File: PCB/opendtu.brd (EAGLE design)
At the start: 104.1 x 54 mm, 11 parts, among them M1 DISPLAY-OLED-128X64-I2CNH, M3 NRF24L01-PA-EXT, X1 MCV1,5/2G

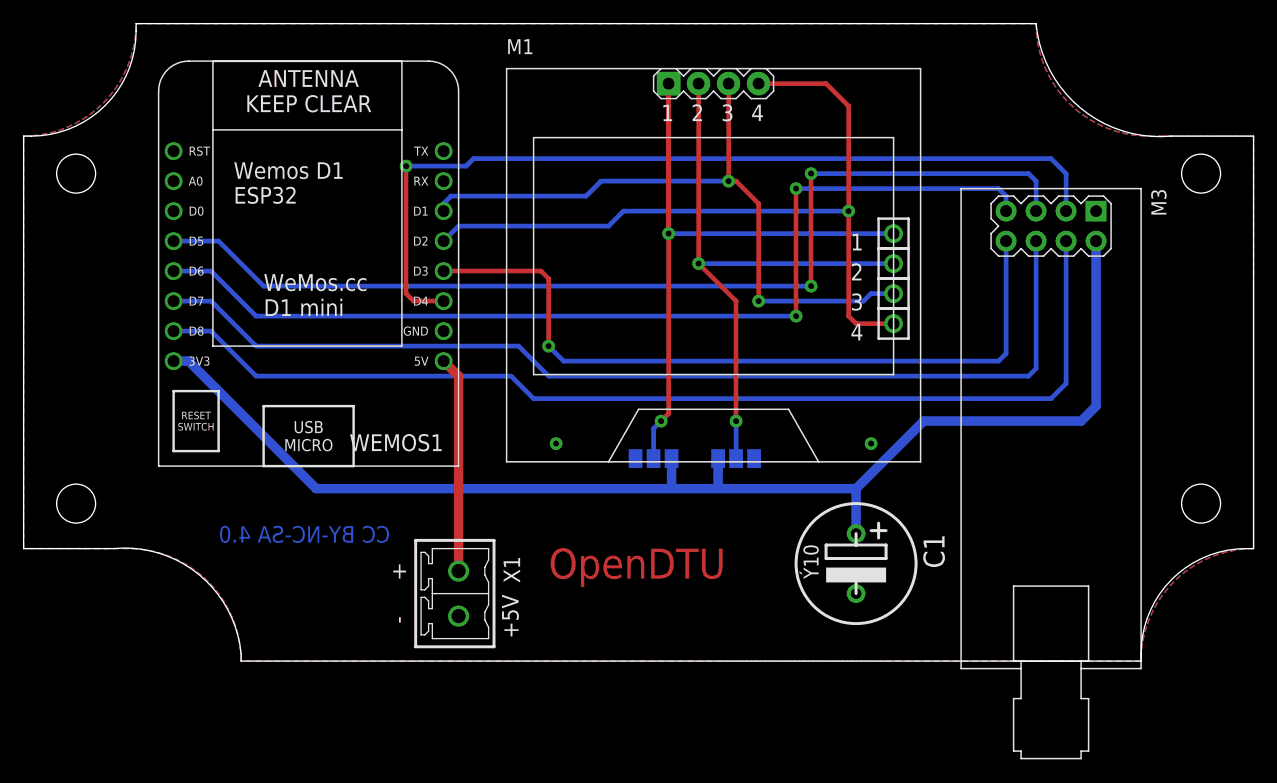
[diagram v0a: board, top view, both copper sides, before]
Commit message: masse
Masse Via hinzugefügt
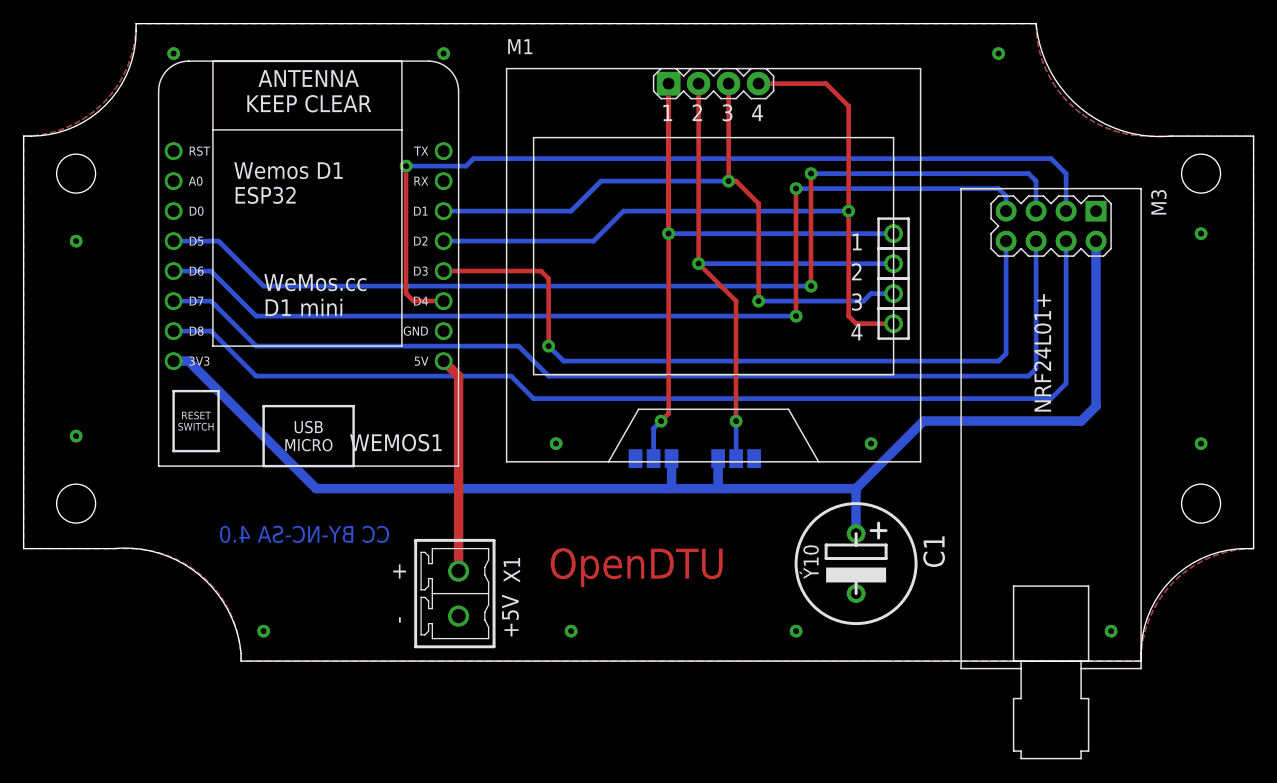
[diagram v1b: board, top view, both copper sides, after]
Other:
- board text added: "NRF24L01+"
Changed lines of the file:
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@@
 <layers>
 <layer number="16" name="Solder" color="1" fill="1" visible="yes" active="yes"/>
-<layer number="1" name="Component" color="4" fill="1" visible="yes" active="yes"/>
+<layer number="1" name="Component" color="4" fill="1" visible="no" active="yes"/>
 <layer number="17" name="Pads" color="2" fill="1" visible="yes" active="yes"/>
 <layer number="18" name="Vias" color="2" fill="1" visible="yes" active="yes"/>
@@
 <text x="59.69" y="46.355" size="1.4" layer="25" ratio="15">3</text>
 <text x="62.23" y="46.355" size="1.4" layer="25" ratio="15">4</text>
+<text x="87.63" y="21.59" size="1.4" layer="25" ratio="15" rot="R90">NRF24L01+</text>
 </plain>
 <attributes>
@@
 <contactref element="M1" pad="4"/>
 <wire x1="71.12" y1="29.21" x2="74.295" y2="29.21" width="0.4" layer="1"/>
-<wire x1="37.465" y1="37.465" x2="50.165" y2="37.465" width="0.4" layer="16"/>
-<wire x1="50.165" y1="37.465" x2="51.435" y2="38.735" width="0.4" layer="16"/>
+<wire x1="48.895" y1="36.195" x2="51.435" y2="38.735" width="0.4" layer="16"/>
 <wire x1="51.435" y1="38.735" x2="70.485" y2="38.735" width="0.4" layer="16"/>
 <via x="70.485" y="38.735" extent="1-16" drill="0.5" diameter="1.1"/>
@@
 <wire x1="70.485" y1="47.625" x2="70.485" y2="38.735" width="0.4" layer="1"/>
 <contactref element="WEMOS1" pad="D2"/>
-<wire x1="36.195" y1="36.195" x2="37.465" y2="37.465" width="0.4" layer="16"/>
+<wire x1="36.195" y1="36.195" x2="48.895" y2="36.195" width="0.4" layer="16"/>
 </signal>
 <signal name="N$2">
 <contactref element="M1" pad="3"/>
 <contactref element="3" pad="1"/>
-<wire x1="36.195" y1="39.37" x2="36.83" y2="40.005" width="0.4" layer="16"/>
-<wire x1="36.83" y1="40.005" x2="48.26" y2="40.005" width="0.4" layer="16"/>
-<wire x1="48.26" y1="40.005" x2="49.53" y2="41.275" width="0.4" layer="16"/>
+<wire x1="36.195" y1="38.735" x2="46.99" y2="38.735" width="0.4" layer="16"/>
+<wire x1="46.99" y1="38.735" x2="49.53" y2="41.275" width="0.4" layer="16"/>
 <wire x1="49.53" y1="41.275" x2="60.325" y2="41.275" width="0.4" layer="16"/>
 <via x="60.325" y="41.275" extent="1-16" drill="0.5" diameter="1.1"/>
@@
 <wire x1="60.96" y1="41.275" x2="60.325" y2="41.275" width="0.4" layer="1"/>
 <contactref element="WEMOS1" pad="D1"/>
-<wire x1="36.195" y1="39.37" x2="36.195" y2="38.735" width="0.4" layer="16"/>
 </signal>
 <signal name="N$3">
@@
 <contactref element="C1" pad="-"/>
 <contactref element="X1" pad="2"/>
-<wire x1="72.39" y1="19.05" x2="91.44" y2="38.735" width="0" layer="19" extent="1-1"/>
-<wire x1="62.484" y1="17.78" x2="72.39" y2="19.05" width="0" layer="19" extent="16-16"/>
-<wire x1="52.451" y1="17.78" x2="62.484" y2="17.78" width="0" layer="19" extent="16-16"/>
-<wire x1="45.72" y1="19.05" x2="52.451" y2="17.78" width="0" layer="19" extent="16-16"/>
-<wire x1="71.12" y1="6.35" x2="72.39" y2="19.05" width="0" layer="19" extent="1-1"/>
-<wire x1="36.195" y1="28.575" x2="45.72" y2="19.05" width="0" layer="19" extent="1-1"/>
-<wire x1="37.465" y1="4.445" x2="45.72" y2="19.05" width="0" layer="19" extent="1-1"/>
+<via x="13.335" y="52.07" extent="1-16" drill="0.5" diameter="1.1"/>
+<via x="83.185" y="52.07" extent="1-16" drill="0.5" diameter="1.1"/>
+<via x="20.955" y="3.175" extent="1-16" drill="0.5" diameter="1.1"/>
+<via x="92.71" y="3.175" extent="1-16" drill="0.5" diameter="1.1"/>
+<via x="5.08" y="19.685" extent="1-16" drill="0.5" diameter="1.1"/>
+<via x="5.08" y="36.195" extent="1-16" drill="0.5" diameter="1.1"/>
+<via x="36.195" y="52.07" extent="1-16" drill="0.5" diameter="1.1"/>
+<via x="100.33" y="36.83" extent="1-16" drill="0.5" diameter="1.1"/>
+<via x="100.33" y="19.05" extent="1-16" drill="0.5" diameter="1.1"/>
+<via x="66.04" y="3.175" extent="1-16" drill="0.5" diameter="1.1"/>
+<via x="46.99" y="3.175" extent="1-16" drill="0.5" diameter="1.1"/>
 </signal>
 </signals>

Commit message: Gerber V1.1
V1.1 vom Gerber
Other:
- board text added: "OpenDTU 3.3.2023 V1.1 Florian Schoop CC BY-NC-SA 4.0"
- board text removed: "OpenDTU 24.2.2023 Florian Schoop CC BY-NC-SA 4.0"
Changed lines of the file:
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@@
 <layers>
 <layer number="16" name="Solder" color="1" fill="1" visible="yes" active="yes"/>
-<layer number="1" name="Component" color="4" fill="1" visible="no" active="yes"/>
+<layer number="1" name="Component" color="4" fill="1" visible="yes" active="yes"/>
 <layer number="17" name="Pads" color="2" fill="1" visible="yes" active="yes"/>
 <layer number="18" name="Vias" color="2" fill="1" visible="yes" active="yes"/>
@@
 J2   2-3  2 +</text>
 <text x="102.87" y="36.195" size="1.4" layer="26" ratio="15" rot="MR270">OpenDTU
-24.2.2023
+3.3.2023 V1.1
 Florian Schoop
 CC BY-NC-SA 4.0</text>
@@
 <text x="62.23" y="46.355" size="1.4" layer="25" ratio="15">4</text>
 <text x="87.63" y="21.59" size="1.4" layer="25" ratio="15" rot="R90">NRF24L01+</text>
+<wire x1="90.17" y1="18.415" x2="90.17" y2="17.145" width="0.4" layer="21"/>
+<wire x1="90.17" y1="17.145" x2="90.17" y2="12.065" width="0.4" layer="21"/>
+<wire x1="90.17" y1="12.065" x2="88.9" y2="12.065" width="0.4" layer="21"/>
+<wire x1="88.9" y1="12.065" x2="88.9" y2="15.875" width="0.4" layer="21"/>
+<wire x1="88.9" y1="15.875" x2="87.63" y2="15.875" width="0.4" layer="21"/>
+<wire x1="87.63" y1="15.875" x2="87.63" y2="12.065" width="0.4" layer="21"/>
+<wire x1="87.63" y1="12.065" x2="86.36" y2="12.065" width="0.4" layer="21"/>
+<wire x1="86.36" y1="12.065" x2="86.36" y2="15.875" width="0.4" layer="21"/>
+<wire x1="86.36" y1="15.875" x2="85.09" y2="15.875" width="0.4" layer="21"/>
+<wire x1="85.09" y1="15.875" x2="85.09" y2="12.065" width="0.4" layer="21"/>
+<wire x1="85.09" y1="12.065" x2="83.82" y2="12.065" width="0.4" layer="21"/>
+<wire x1="83.82" y1="12.065" x2="83.82" y2="15.875" width="0.4" layer="21"/>
+<wire x1="83.82" y1="15.875" x2="82.55" y2="15.875" width="0.4" layer="21"/>
+<wire x1="82.55" y1="15.875" x2="82.55" y2="12.065" width="0.4" layer="21"/>
+<wire x1="82.55" y1="12.065" x2="80.01" y2="12.065" width="0.4" layer="21"/>
+<wire x1="83.82" y1="17.145" x2="90.17" y2="17.145" width="0.4" layer="21"/>
+<wire x1="80.01" y1="17.78" x2="95.25" y2="17.78" width="0.1" layer="21"/>
+<wire x1="80.01" y1="11.43" x2="95.25" y2="11.43" width="0.1" layer="21"/>
 </plain>
 <attributes>
@@
 <via x="66.04" y="3.175" extent="1-16" drill="0.5" diameter="1.1"/>
 <via x="46.99" y="3.175" extent="1-16" drill="0.5" diameter="1.1"/>
+<wire x1="91.44" y1="38.735" x2="100.33" y2="36.83" width="0" layer="19" extent="1-1"/>
+<wire x1="83.185" y1="52.07" x2="91.44" y2="38.735" width="0" layer="19" extent="1-1"/>
+<wire x1="100.33" y1="19.05" x2="100.33" y2="36.83" width="0" layer="19" extent="1-1"/>
+<wire x1="92.71" y1="3.175" x2="100.33" y2="19.05" width="0" layer="19" extent="1-1"/>
+<wire x1="71.12" y1="6.35" x2="92.71" y2="3.175" width="0" layer="19" extent="1-1"/>
+<wire x1="66.04" y1="3.175" x2="71.12" y2="6.35" width="0" layer="19" extent="1-1"/>
+<wire x1="72.39" y1="19.05" x2="71.12" y2="6.35" width="0" layer="19" extent="1-1"/>
+<wire x1="62.484" y1="17.78" x2="72.39" y2="19.05" width="0" layer="19" extent="16-16"/>
+<wire x1="52.451" y1="17.78" x2="62.484" y2="17.78" width="0" layer="19" extent="16-16"/>
+<wire x1="45.72" y1="19.05" x2="52.451" y2="17.78" width="0" layer="19" extent="16-16"/>
+<wire x1="36.195" y1="28.575" x2="45.72" y2="19.05" width="0" layer="19" extent="1-1"/>
+<wire x1="46.99" y1="3.175" x2="52.451" y2="17.78" width="0" layer="19" extent="16-16"/>
+<wire x1="37.465" y1="4.445" x2="46.99" y2="3.175" width="0" layer="19" extent="1-1"/>
+<wire x1="20.955" y1="3.175" x2="37.465" y2="4.445" width="0" layer="19" extent="1-1"/>
+<wire x1="5.08" y1="19.685" x2="20.955" y2="3.175" width="0" layer="19" extent="1-1"/>
+<wire x1="5.08" y1="36.195" x2="5.08" y2="19.685" width="0" layer="19" extent="1-1"/>
+<wire x1="13.335" y1="52.07" x2="5.08" y2="36.195" width="0" layer="19" extent="1-1"/>
+<wire x1="36.195" y1="52.07" x2="13.335" y2="52.07" width="0" layer="19" extent="1-1"/>
 </signal>
 </signals>

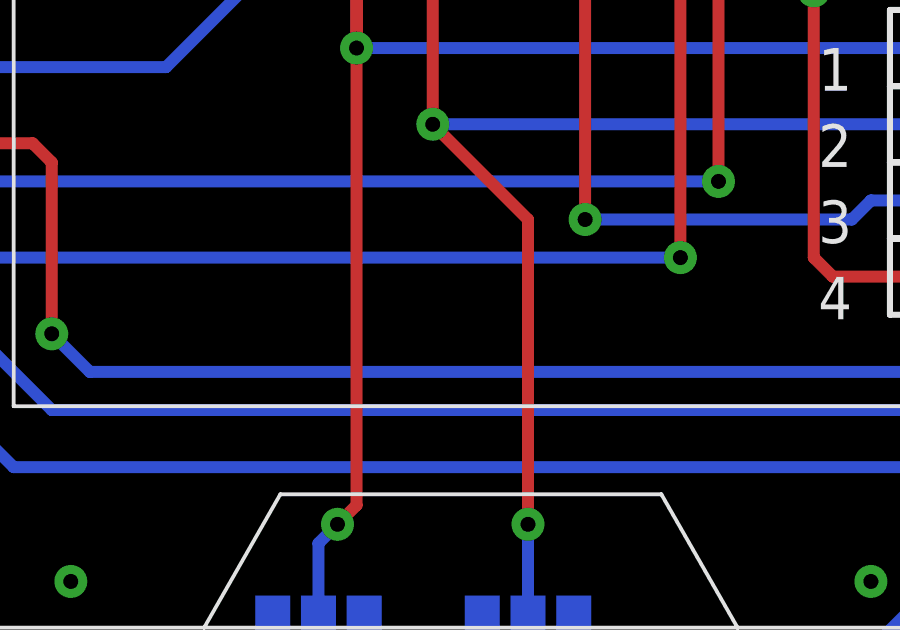
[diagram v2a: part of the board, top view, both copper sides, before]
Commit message: V1.1
Text nochmal etwas verschoben. PDF vom Schaltplan hinzugefügt.
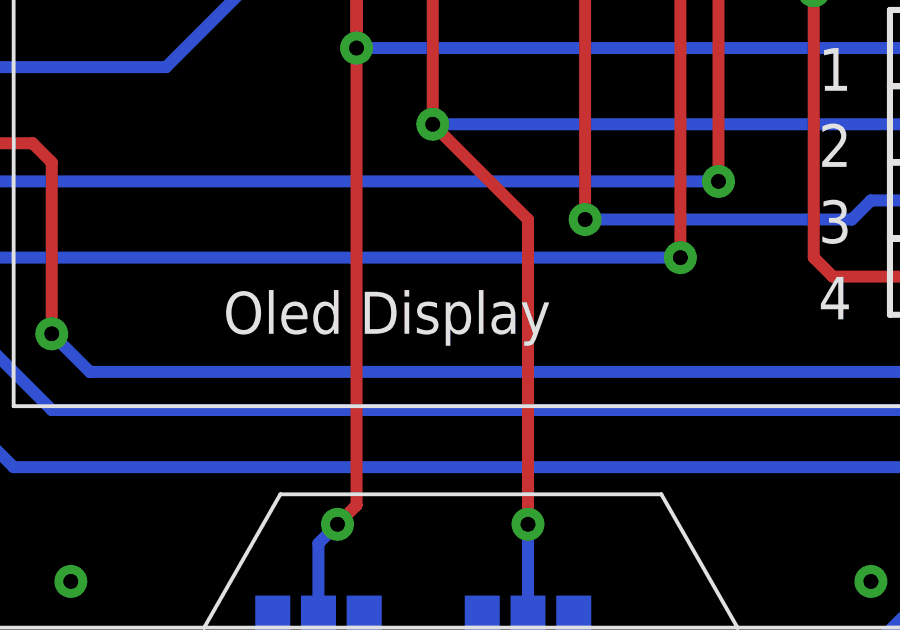
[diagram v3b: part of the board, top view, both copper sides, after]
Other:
- board text added: "Oled Display"
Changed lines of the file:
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@@
 J1   2-3  1 -
 J2   2-3  2 +</text>
-<text x="102.87" y="36.195" size="1.4" layer="26" ratio="15" rot="MR270">OpenDTU
+<text x="101.6" y="38.735" size="1.4" layer="26" ratio="15" rot="MR270">OpenDTU
 3.3.2023 V1.1
 Florian Schoop
@@
 <wire x1="80.01" y1="17.78" x2="95.25" y2="17.78" width="0.1" layer="21"/>
 <wire x1="80.01" y1="11.43" x2="95.25" y2="11.43" width="0.1" layer="21"/>
+<text x="50.8" y="27.305" size="1.4" layer="25" ratio="15">Oled Display</text>
 </plain>
 <attributes>
@@
 <via x="66.04" y="3.175" extent="1-16" drill="0.5" diameter="1.1"/>
 <via x="46.99" y="3.175" extent="1-16" drill="0.5" diameter="1.1"/>
-<wire x1="91.44" y1="38.735" x2="100.33" y2="36.83" width="0" layer="19" extent="1-1"/>
-<wire x1="83.185" y1="52.07" x2="91.44" y2="38.735" width="0" layer="19" extent="1-1"/>
-<wire x1="100.33" y1="19.05" x2="100.33" y2="36.83" width="0" layer="19" extent="1-1"/>
-<wire x1="92.71" y1="3.175" x2="100.33" y2="19.05" width="0" layer="19" extent="1-1"/>
-<wire x1="71.12" y1="6.35" x2="92.71" y2="3.175" width="0" layer="19" extent="1-1"/>
-<wire x1="66.04" y1="3.175" x2="71.12" y2="6.35" width="0" layer="19" extent="1-1"/>
-<wire x1="72.39" y1="19.05" x2="71.12" y2="6.35" width="0" layer="19" extent="1-1"/>
-<wire x1="62.484" y1="17.78" x2="72.39" y2="19.05" width="0" layer="19" extent="16-16"/>
-<wire x1="52.451" y1="17.78" x2="62.484" y2="17.78" width="0" layer="19" extent="16-16"/>
-<wire x1="45.72" y1="19.05" x2="52.451" y2="17.78" width="0" layer="19" extent="16-16"/>
-<wire x1="36.195" y1="28.575" x2="45.72" y2="19.05" width="0" layer="19" extent="1-1"/>
-<wire x1="46.99" y1="3.175" x2="52.451" y2="17.78" width="0" layer="19" extent="16-16"/>
-<wire x1="37.465" y1="4.445" x2="46.99" y2="3.175" width="0" layer="19" extent="1-1"/>
-<wire x1="20.955" y1="3.175" x2="37.465" y2="4.445" width="0" layer="19" extent="1-1"/>
-<wire x1="5.08" y1="19.685" x2="20.955" y2="3.175" width="0" layer="19" extent="1-1"/>
-<wire x1="5.08" y1="36.195" x2="5.08" y2="19.685" width="0" layer="19" extent="1-1"/>
-<wire x1="13.335" y1="52.07" x2="5.08" y2="36.195" width="0" layer="19" extent="1-1"/>
-<wire x1="36.195" y1="52.07" x2="13.335" y2="52.07" width="0" layer="19" extent="1-1"/>
 </signal>
 </signals>
